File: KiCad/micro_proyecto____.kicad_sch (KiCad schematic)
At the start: 12 parts, among them J1 Conn_01x03, J2 Conn_01x05, SW1 SW_Push, U2 PIC24HJ128GP502, Y1 Crystal

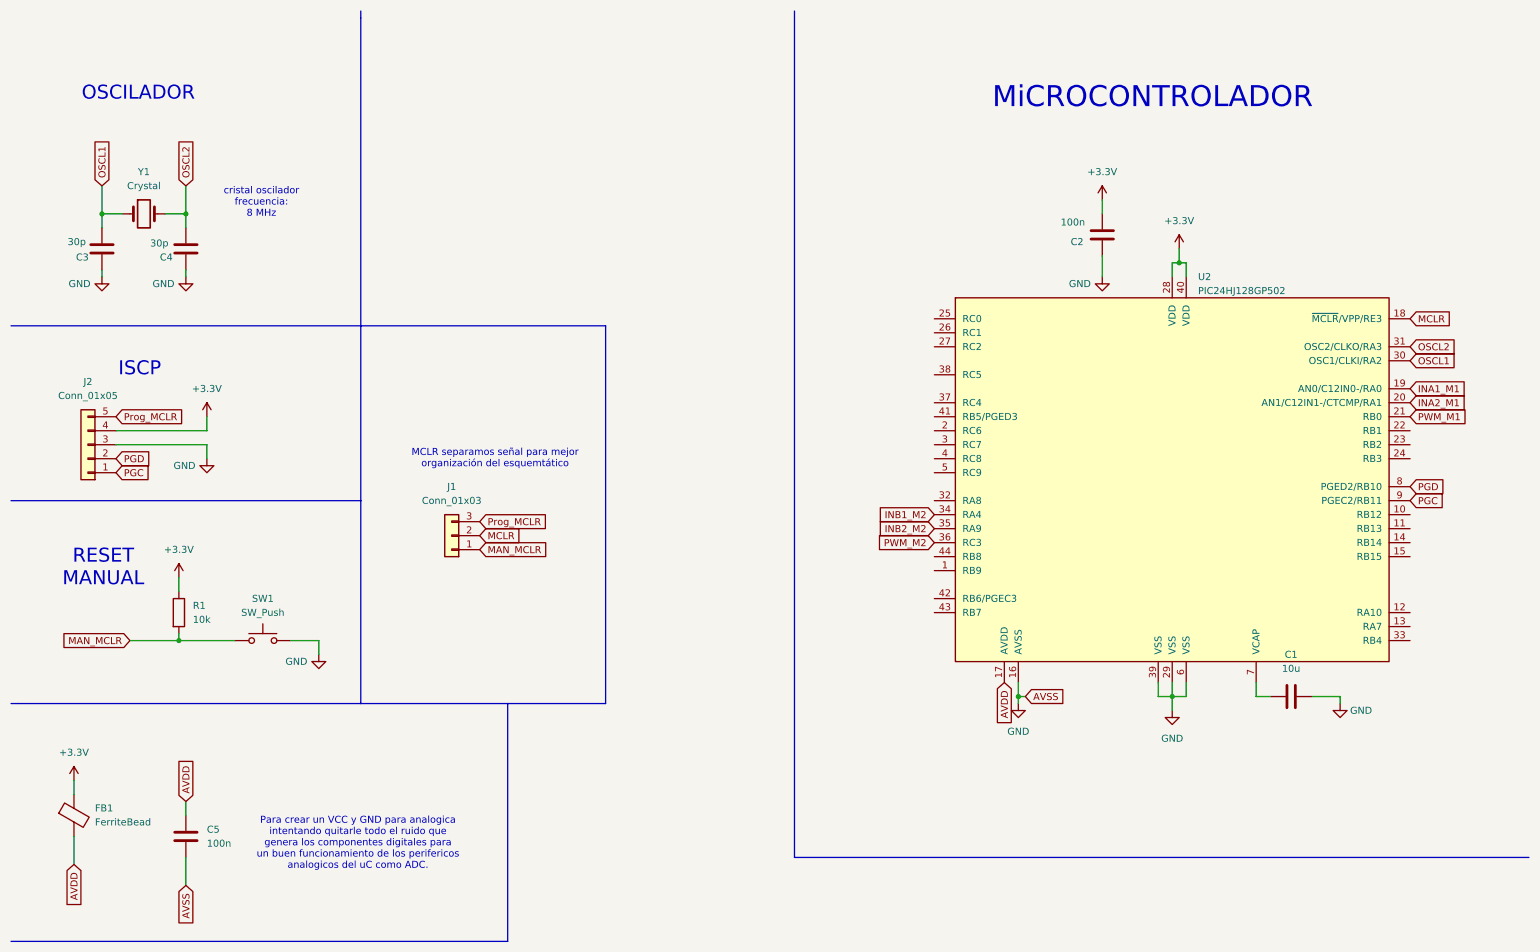
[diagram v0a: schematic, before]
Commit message: Poner parte digital
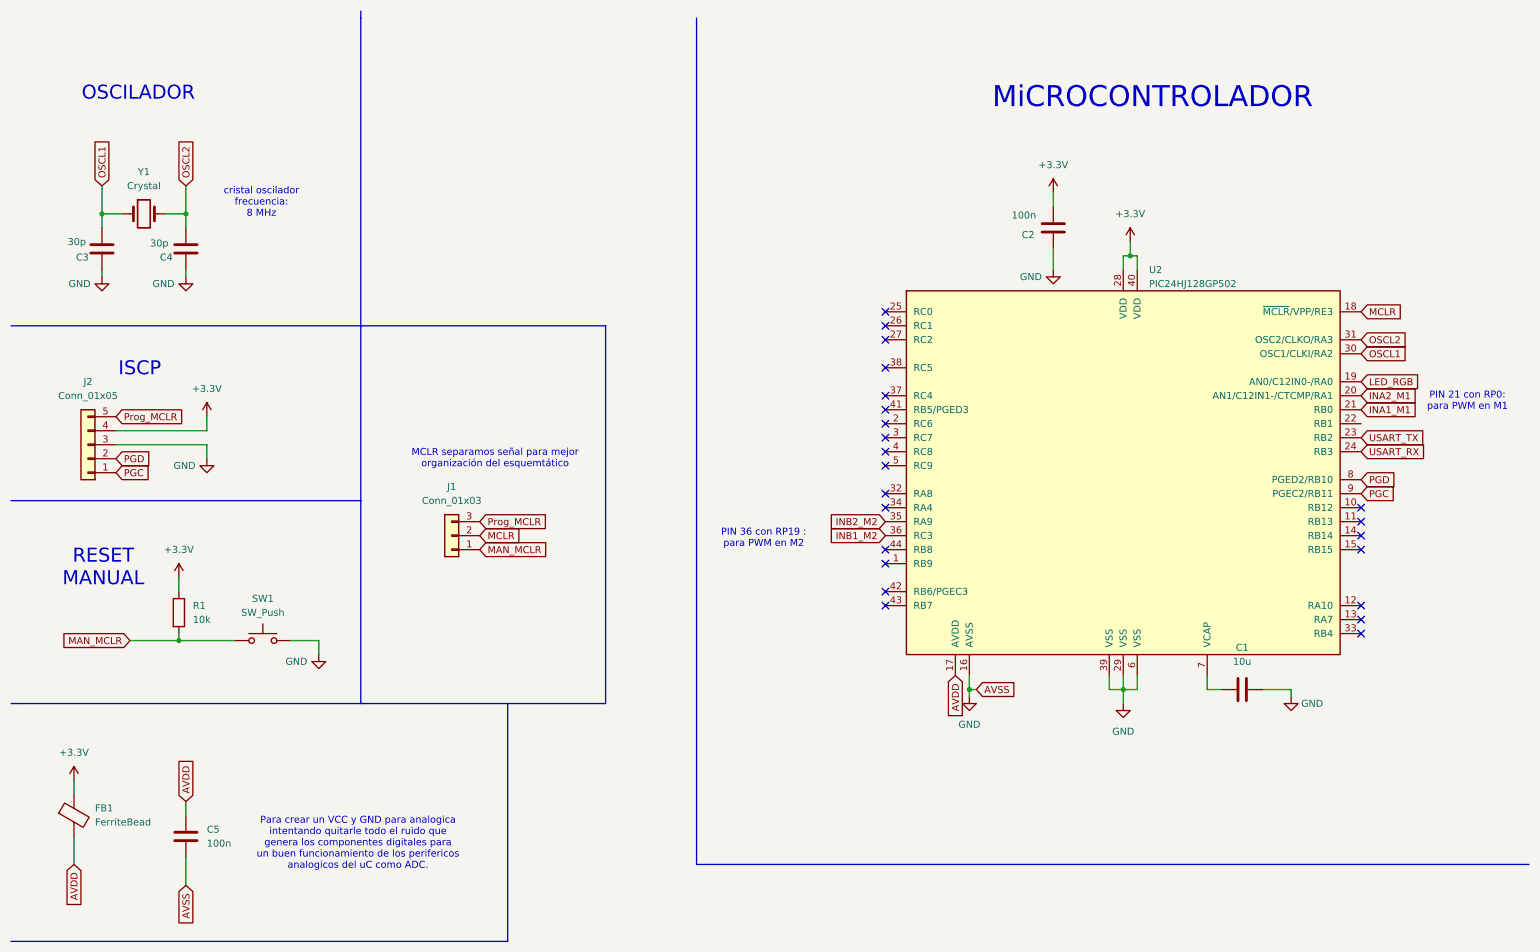
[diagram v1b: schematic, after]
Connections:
- net PWM_M1 is gone; now on net INA1_M1: U2.21 (RB0)
- net PWM_M2 is gone; now on net INB1_M2: U2.36 (RC3)
- net INA1_M1: no longer U2.19 (AN0/C12IN0-/RA0)
- net INB1_M2: no longer U2.34 (NC)
- net USART_TX: now reaches U2.23 (RB2)
- net USART_RX: now reaches U2.24 (RB3)
- new net LED_RGB: U2.19 (AN0/C12IN0-/RA0)
- no-connect marks 0 -> 23
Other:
- note added: "PIN 21 con RP0: para PWM en M1"
- note added: "PIN 36 con RP19 : para PWM en M2"
- moved on the sheet: C1, C2, U2
